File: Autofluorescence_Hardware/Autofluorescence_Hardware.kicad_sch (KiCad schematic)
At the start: 29 parts, among them U1 PAM2863ECR, U2 PAM2863ECR, U3 PAM2863ECR

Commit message: Finished layout
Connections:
- net GND: now also D1.3, D4.3, D6.3
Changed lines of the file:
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@@
 	)
 	(junction
+		(at 109.22 138.43)
+		(diameter 0)
+		(color 0 0 0 0)
+	)
+	(junction
 		(at 105.41 77.47)
 		(diameter 0)
@@
 	)
 	(junction
+		(at 109.22 43.18)
+		(diameter 0)
+		(color 0 0 0 0)
+	)
+	(junction
 		(at 102.87 45.72)
 		(diameter 0)
@@
 	)
 	(junction
+		(at 109.22 90.17)
+		(diameter 0)
+		(color 0 0 0 0)
+	)
+	(junction
 		(at 48.26 48.26)
 		(diameter 0)
@@
 	(wire
 		(pts
+			(xy 109.22 85.09) (xy 109.22 90.17)
+		)
+		(stroke
+			(width 0)
+			(type default)
+		)
+	)
+	(wire
+		(pts
 			(xy 54.61 30.48) (xy 105.41 30.48)
 		)
@@
 	(wire
 		(pts
+			(xy 109.22 38.1) (xy 109.22 43.18)
+		)
+		(stroke
+			(width 0)
+			(type default)
+		)
+	)
+	(wire
+		(pts
 			(xy 137.16 77.47) (xy 137.16 83.82)
 		)
@@
 	(wire
 		(pts
+			(xy 119.38 38.1) (xy 109.22 38.1)
+		)
+		(stroke
+			(width 0)
+			(type default)
+		)
+	)
+	(wire
+		(pts
 			(xy 38.1 125.73) (xy 38.1 123.19)
 		)
@@
 	(wire
 		(pts
+			(xy 109.22 133.35) (xy 109.22 138.43)
+		)
+		(stroke
+			(width 0)
+			(type default)
+		)
+	)
+	(wire
+		(pts
 			(xy 54.61 125.73) (xy 54.61 140.97)
 		)
@@
 	(wire
 		(pts
+			(xy 119.38 133.35) (xy 109.22 133.35)
+		)
+		(stroke
+			(width 0)
+			(type default)
+		)
+	)
+	(wire
+		(pts
 			(xy 102.87 90.17) (xy 109.22 90.17)
 		)
@@
 	(wire
 		(pts
+			(xy 119.38 85.09) (xy 109.22 85.09)
+		)
+		(stroke
+			(width 0)
+			(type default)
+		)
+	)
+	(wire
+		(pts
 			(xy 102.87 90.17) (xy 102.87 92.71)
 		)
@@
 		(pin "1"
 		)
+		(pin "3"
+		)
 		(instances
 			(project "Autofluorescence_Hardware"
@@
 	)
 	(symbol
+		(lib_name "D_2")
 		(lib_id "Device:D")
 		(at 121.92 85.09 90)
@@
 		(pin "1"
 		)
+		(pin "3"
+		)
 		(instances
 			(project "Autofluorescence_Hardware"
@@
 	)
 	(symbol
+		(lib_name "D_1")
 		(lib_id "Device:D")
 		(at 121.92 38.1 90)
@@
 		(pin "1"
 		)
+		(pin "3"
+		)
 		(instances

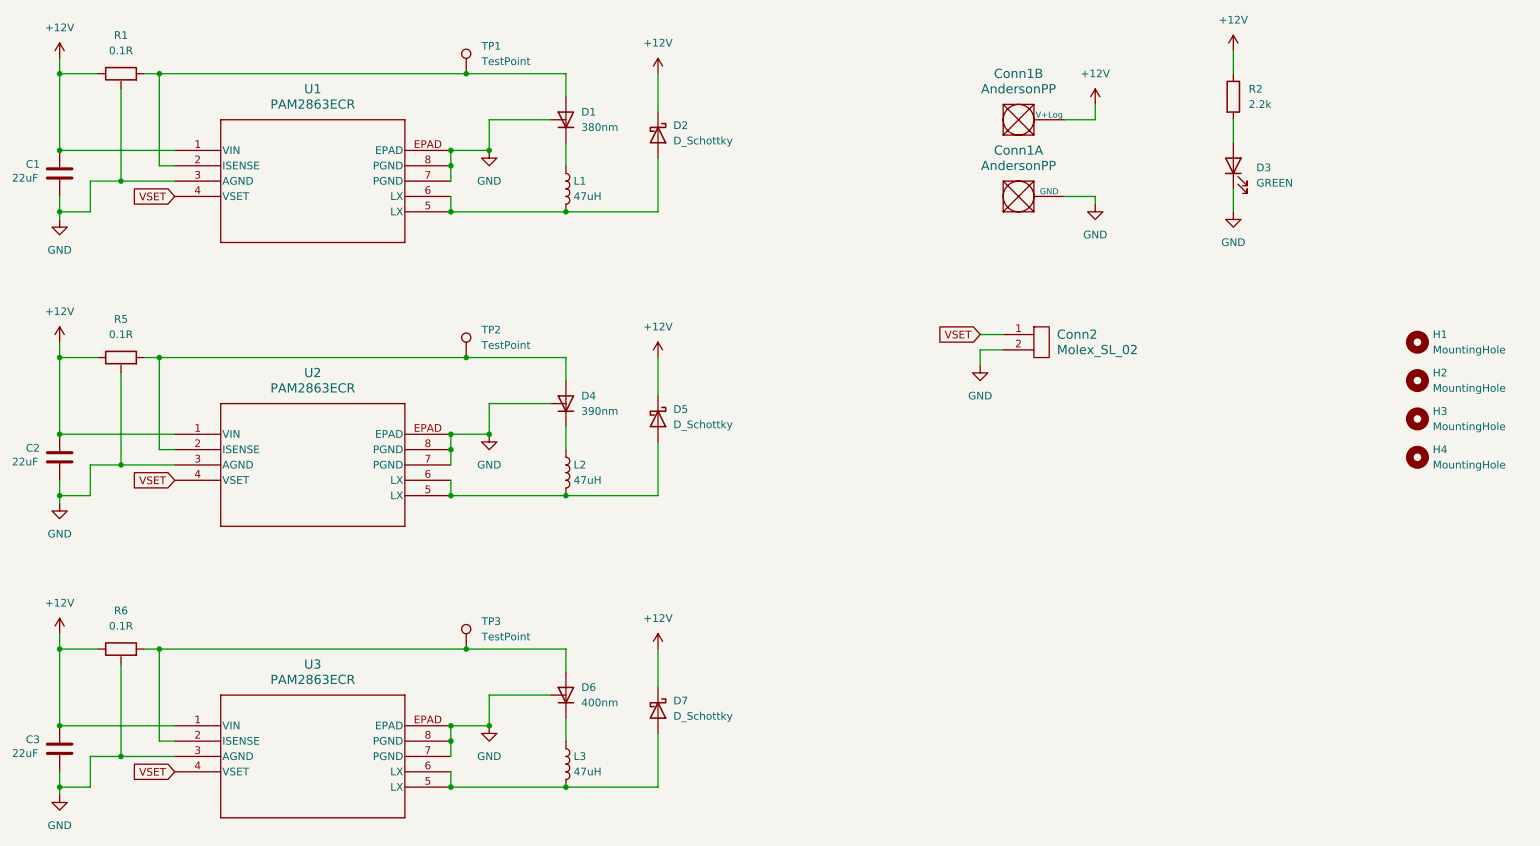
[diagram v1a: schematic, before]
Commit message: Fixed for aluminum core pcb
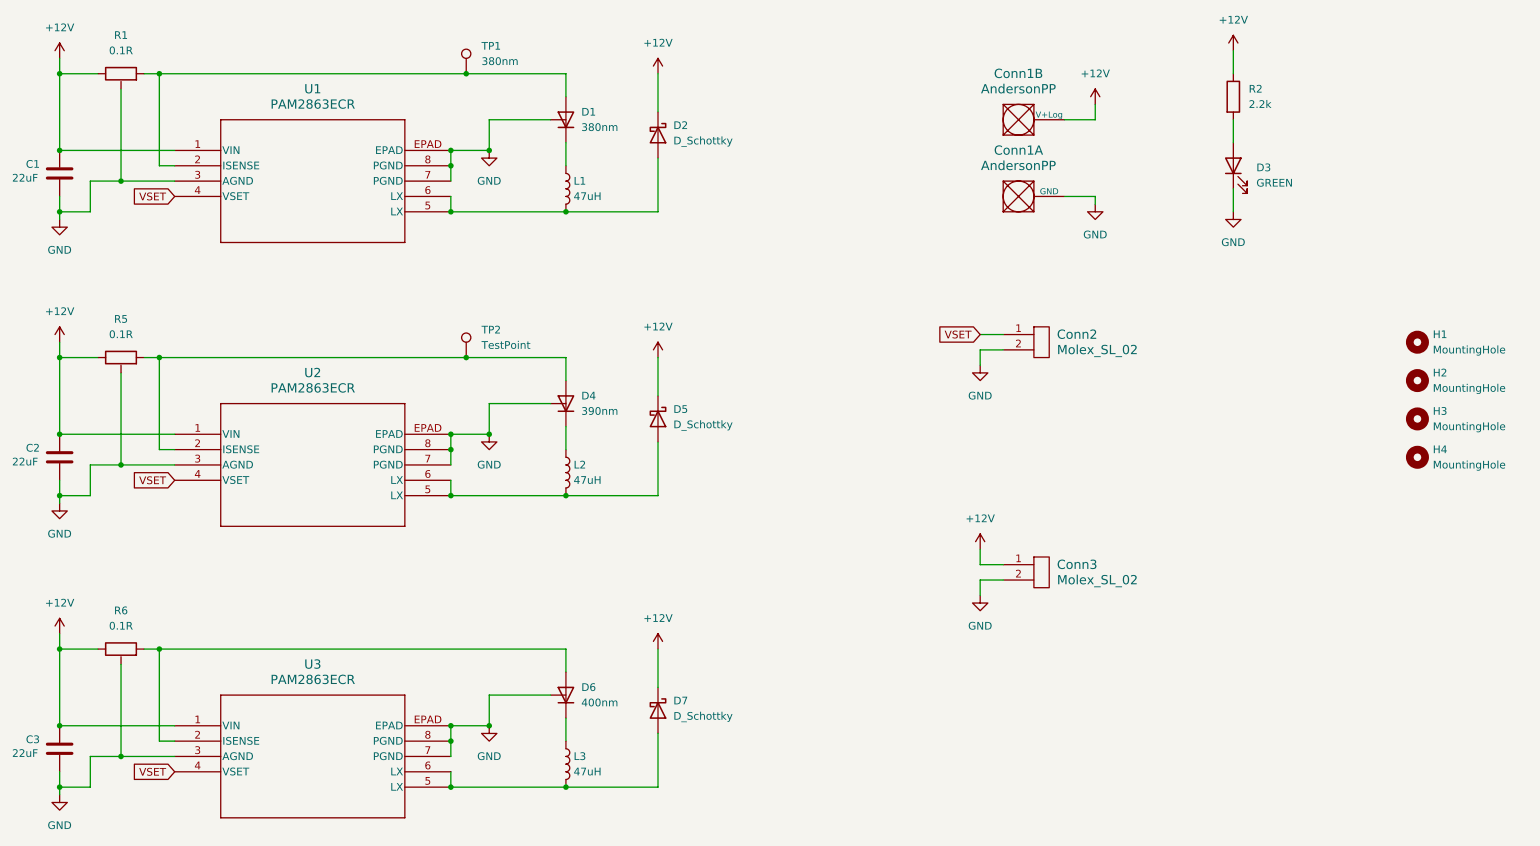
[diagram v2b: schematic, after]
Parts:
- removed TP3: TestPoint, symbol Connector:TestPoint
- added Conn3: Molex_SL_02, MRDT_Connectors:MOLEX_SL_02_Horizontal, symbol MRDT_Connectors:Molex_SL_02
- Conn1: footprint MRDT_Connectors:Anderson_2_Horizontal_Side_by_Side -> MRDT_Connectors:Square_Anderson_2_H_Side_By_Side
- Conn2: footprint MRDT_Connectors:MOLEX_SL_02_Vertical -> MRDT_Connectors:MOLEX_SL_02_Horizontal
- TP1: value TestPoint -> 380nm; footprint (none) -> TestPoint:TestPoint_Pad_D1.5mm
- TP2: footprint (none) -> TestPoint:TestPoint_Pad_D1.5mm
- U1, U2, U3: footprint SOIC_863ECR_DIO -> autofluorescence_board:SOIC_863ECR_DIO
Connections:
- net +12V: now also Conn3.1
- net GND: now also Conn3.2
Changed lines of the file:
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@@
 	)
 	(junction
-		(at 105.41 125.73)
-		(diameter 0)
-		(color 0 0 0 0)
-	)
-	(junction
 		(at 102.87 100.33)
 		(diameter 0)
@@
 	(wire
 		(pts
+			(xy 194.31 114.3) (xy 190.5 114.3)
+		)
+		(stroke
+			(width 0)
+			(type default)
+		)
+	)
+	(wire
+		(pts
 			(xy 38.1 138.43) (xy 57.15 138.43)
 		)
@@
 	(wire
 		(pts
+			(xy 190.5 111.76) (xy 194.31 111.76)
+		)
+		(stroke
+			(width 0)
+			(type default)
+		)
+	)
+	(wire
+		(pts
 			(xy 137.16 125.73) (xy 137.16 132.08)
 		)
@@
 	(wire
 		(pts
-			(xy 105.41 125.73) (xy 121.92 125.73)
+			(xy 54.61 125.73) (xy 121.92 125.73)
 		)
 		(stroke
@@
 	(wire
 		(pts
-			(xy 54.61 125.73) (xy 105.41 125.73)
+			(xy 190.5 109.22) (xy 190.5 111.76)
 		)
 		(stroke
@@
 	(wire
 		(pts
+			(xy 190.5 114.3) (xy 190.5 116.84)
+		)
+		(stroke
+			(width 0)
+			(type default)
+		)
+	)
+	(wire
+		(pts
 			(xy 121.92 137.16) (xy 121.92 140.97)
 		)
@@
 			)
 		)
-		(property "Footprint" "MRDT_Connectors:Anderson_2_Horizontal_Side_by_Side"
+		(property "Footprint" "MRDT_Connectors:Square_Anderson_2_H_Side_By_Side"
 			(at 190.5 67.31 0)
 			(effects
@@
 			)
 		)
-		(property "Footprint" "SOIC_863ECR_DIO"
+		(property "Footprint" "autofluorescence_board:SOIC_863ECR_DIO"
 			(at 57.15 90.17 0)
 			(effects
@@
 			)
 		)
-		(property "Footprint" "MRDT_Connectors:MOLEX_SL_02_Vertical"
+		(property "Footprint" "MRDT_Connectors:MOLEX_SL_02_Horizontal"
 			(at 199.39 80.01 0)
 			(effects
@@
 			)
 		)
-		(property "Footprint" "SOIC_863ECR_DIO"
+		(property "Footprint" "autofluorescence_board:SOIC_863ECR_DIO"
 			(at 57.15 138.43 0)
 			(effects
@@
 	)
 	(symbol
+		(lib_id "MRDT_Connectors:Molex_SL_02")
+		(at 199.39 115.57 0)
+		(unit 1)
+		(exclude_from_sim no)
+		(in_bom yes)
+		(on_board yes)
+		(dnp no)
+		(fields_autoplaced yes)
+		(property "Reference" "Conn3"
+			(at 203.2 111.7599 0)
+			(effects
+				(font
+					(size 1.524 1.524)
+				)
+				(justify left)
+			)
+		)
+		(property "Value" "Molex_SL_02"
+			(at 203.2 114.2999 0)
+			(effects
+				(font
+					(size 1.524 1.524)
+				)
+				(justify left)
+			)
+		)
+		(property "Footprint" "MRDT_Connectors:MOLEX_SL_02_Horizontal"
+			(at 199.39 118.11 0)
+			(effects
+				(font
+					(size 1.524 1.524)
+				)
+				(hide yes)
+			)
+		)
+		(property "Datasheet" ""
+			(at 199.39 118.11 0)
+			(effects
+				(font
+					(size 1.524 1.524)
+				)
+				(hide yes)
+			)
+		)
+		(property "Description" ""
+			(at 199.39 115.57 0)
+			(effects
+				(font
+					(size 1.27 1.27)
+				)
+				(hide yes)
+			)
+		)
+		(pin "1"
+		)
+		(pin "2"
+		)
+		(instances
+			(project "Autofluorescence_Hardware"
+				(path "/15bff5d8-5567-4731-9b94-d21a53ee51ce"
+					(reference "Conn3")
+					(unit 1)
+				)
+			)
+		)
+	)
+	(symbol
 		(lib_id "Device:LED")
 		(at 232.41 45.72 90)
@@
 			)
 		)
-		(property "Footprint" ""
+		(property "Footprint" "TestPoint:TestPoint_Pad_D1.5mm"
 			(at 110.49 77.47 0)
 			(effects
@@
 			)
 		)
-		(property "Value" "TestPoint"
+		(property "Value" "380nm"
 			(at 107.95 28.4479 0)
 			(effects
@@
 			)
 		)
-		(property "Footprint" ""
+		(property "Footprint" "TestPoint:TestPoint_Pad_D1.5mm"
 			(at 110.49 30.48 0)
 			(effects
@@
 	(symbol
 		(lib_id "power:+12V")
+		(at 190.5 109.22 0)
+		(unit 1)
+		(exclude_from_sim no)
+		(in_bom yes)
+		(on_board yes)
+		(dnp no)
+		(fields_autoplaced yes)
+		(property "Reference" "#PWR019"
+			(at 190.5 113.03 0)
+			(effects
+				(font
+					(size 1.27 1.27)
+				)
+				(hide yes)
+			)
+		)
+		(property "Value" "+12V"
+			(at 190.5 104.14 0)
+			(effects
+				(font
+					(size 1.27 1.27)
+				)
+			)
+		)
+		(property "Footprint" ""
+			(at 190.5 109.22 0)
+			(effects
+				(font
+					(size 1.27 1.27)
+				)
+				(hide yes)
+			)
+		)
+		(property "Datasheet" ""
+			(at 190.5 109.22 0)
+			(effects
+				(font
+					(size 1.27 1.27)
+				)
+				(hide yes)
+			)
+		)
+		(property "Description" "Power symbol creates a global label with name \"+12V\""
+			(at 190.5 109.22 0)
+			(effects
+				(font
+					(size 1.27 1.27)
+				)
+				(hide yes)
+			)
+		)
+		(pin "1"
+		)
+		(instances
+			(project "Autofluorescence_Hardware"
+				(path "/15bff5d8-5567-4731-9b94-d21a53ee51ce"
+					(reference "#PWR019")
+					(unit 1)
+				)
+			)
+		)
+	)
+	(symbol
+		(lib_id "power:+12V")
 		(at 38.1 123.19 0)
 		(unit 1)
@@
 	)
 	(symbol
+		(lib_id "power:GND")
+		(at 190.5 116.84 0)
+		(unit 1)
+		(exclude_from_sim no)
+		(in_bom yes)
+		(on_board yes)
+		(dnp no)
+		(fields_autoplaced yes)
+		(property "Reference" "#PWR018"
+			(at 190.5 123.19 0)
+			(effects
+				(font
+					(size 1.27 1.27)
+				)
+				(hide yes)
+			)
+		)
+		(property "Value" "GND"
+			(at 190.5 121.92 0)
+			(effects
+				(font
+					(size 1.27 1.27)
+				)
+			)
+		)
+		(property "Footprint" ""
+			(at 190.5 116.84 0)
+			(effects
+				(font
+					(size 1.27 1.27)
+				)
+				(hide yes)
+			)
+		)
+		(property "Datasheet" ""
+			(at 190.5 116.84 0)
+			(effects
+				(font
+					(size 1.27 1.27)
+				)
+				(hide yes)
+			)
+		)
+		(property "Description" "Power symbol creates a global label with name \"GND\" , ground"
+			(at 190.5 116.84 0)
+			(effects
+				(font
+					(size 1.27 1.27)
+				)
+				(hide yes)
+			)
+		)
+		(pin "1"
+		)
+		(instances
+			(project "Autofluorescence_Hardware"
+				(path "/15bff5d8-5567-4731-9b94-d21a53ee51ce"
+					(reference "#PWR018")
+					(unit 1)
+				)
+			)
+		)
+	)
+	(symbol
 		(lib_id "autofluorescence_board:PAM2863ECR")
 		(at 57.15 43.18 0)
@@
 			)
 		)
-		(property "Footprint" "SOIC_863ECR_DIO"
+		(property "Footprint" "autofluorescence_board:SOIC_863ECR_DIO"
 			(at 57.15 43.18 0)
 			(effects
@@
 			)
 		)
-		(property "Footprint" "MRDT_Connectors:Anderson_2_Horizontal_Side_by_Side"
+		(property "Footprint" "MRDT_Connectors:Square_Anderson_2_H_Side_By_Side"
 			(at 190.5 54.61 0)
 			(effects
@@
 					(unit 1)
 				)
-			)
-		)
-	)
-	(symbol
-		(lib_id "Connector:TestPoint")
-		(at 105.41 125.73 0)
-		(unit 1)
-		(exclude_from_sim no)
-		(in_bom yes)
-		(on_board yes)
-		(dnp no)
-		(fields_autoplaced yes)
-		(property "Reference" "TP3"
-			(at 107.95 121.1579 0)
-			(effects
-				(font
-					(size 1.27 1.27)
-				)
-				(justify left)
-			)
-		)
-		(property "Value" "TestPoint"
-			(at 107.95 123.6979 0)
-			(effects
-				(font
-					(size 1.27 1.27)
-				)
-				(justify left)
-			)
-		)
-		(property "Footprint" ""
-			(at 110.49 125.73 0)
-			(effects
-				(font
-					(size 1.27 1.27)
-				)
-				(hide yes)
-			)
-		)
-		(property "Datasheet" "~"
-			(at 110.49 125.73 0)
-			(effects
-				(font
-					(size 1.27 1.27)
-				)
-				(hide yes)
-			)
-		)
-		(property "Description" "test point"
-			(at 105.41 125.73 0)
-			(effects
-				(font
-					(size 1.27 1.27)
-				)
-				(hide yes)
-			)
-		)
-		(pin "1"
-		)
-		(instances
-			(project "Autofluorescence_Hardware"
-				(path "/15bff5d8-5567-4731-9b94-d21a53ee51ce"
-					(reference "TP3")
-					(unit 1)
-				)
